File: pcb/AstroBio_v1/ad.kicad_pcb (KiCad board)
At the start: 2 copper layers, 100 x 100 mm, 52 parts, among them J1 POWER 24V, J10 NTC 10k 3950, J12 HEIGHT_SENSOR2, J13 HEIGHT_SENSOR2, J2 Nema17, J3 MS1, J4 MS2, J5 MS2, J6 MS2, J7 FLOW_SENSOR, J8 SERVO, J9 PH_MODUL, U1 ESP32-DevKitC, U2 TBA2-0511, U3 LM3940, U4 LM358

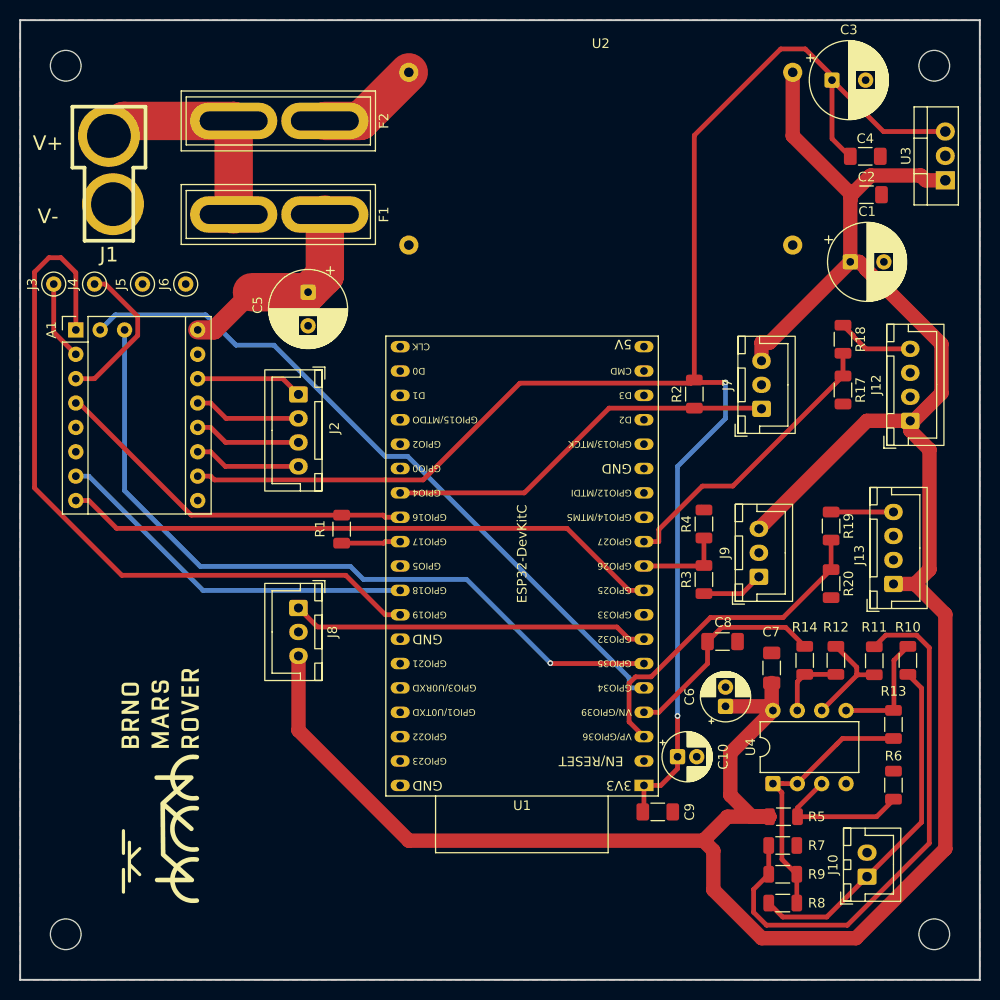
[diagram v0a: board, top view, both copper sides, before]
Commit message: Flip the ESP32 around and generate gerbers
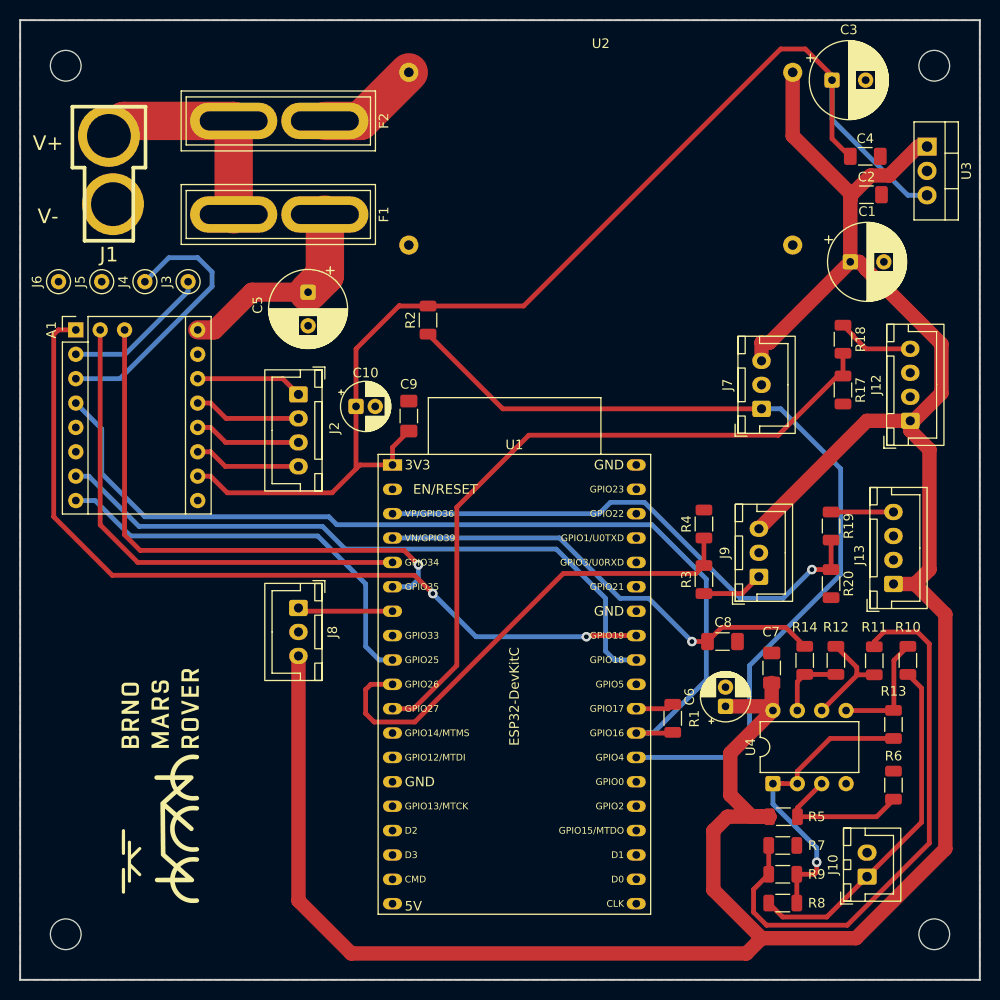
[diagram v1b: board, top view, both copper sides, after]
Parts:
- moved C10 49.5 mm to (76.5, 63.5)
- moved C9 48.7 mm to (82.0, 64.5), turned to 90 degrees
- moved U1 42.4 mm to (80.3, 69.6), turned to 0 degrees
- moved R1 39.7 mm to (109.5, 96.0), turned to -90 degrees
- moved R2 28.8 mm to (84.0, 54.5)
- moved J3 14.0 mm to (59.0, 50.5)
- moved J6 13.3 mm to (45.5, 50.5)
- moved J4 5.26 mm to (54.5, 50.5)
- moved J5 4.26 mm to (50.0, 50.5)
- moved U3 4.00 mm to (136.0, 36.4), turned to -90 degrees
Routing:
- net RX_TMC: track 38.7 -> 100.0 mm
- net SIGNAL_FLOW: track 41.3 -> 93.2 mm
- net +3.3V: track 177.0 -> 129.2 mm, vias 2 -> 0
- net SIGNAL_LEVEL2: track 31.0 -> 73.3 mm
- net SIGNAL_PH: track 9.14 -> 50.8 mm
- net STEP_TMC: track 38.7 -> 69.6 mm
- net SIGNAL_SERVO: track 37.3 -> 9.94 mm
- net SIGNAL_NTC: track 22.6 -> 48.9 mm, vias 0 -> 1
- net DIAG_TMC0: track 74.0 -> 52.4 mm
- net DIAG_TMC1: track 78.3 -> 57.8 mm
- net +5V: track 262.2 -> 282.4 mm
- net SIGNAL_LEVEL1: track 35.5 -> 54.9 mm, vias 0 -> 1
- net DIR_TMC: track 63.1 -> 43.7 mm
- net Net-(A1-MS2): track 16.2 -> 28.3 mm
- net EN_TMC: track 77.6 -> 87.4 mm, vias 0 -> 2
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
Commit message: change the LDO for a smaller one
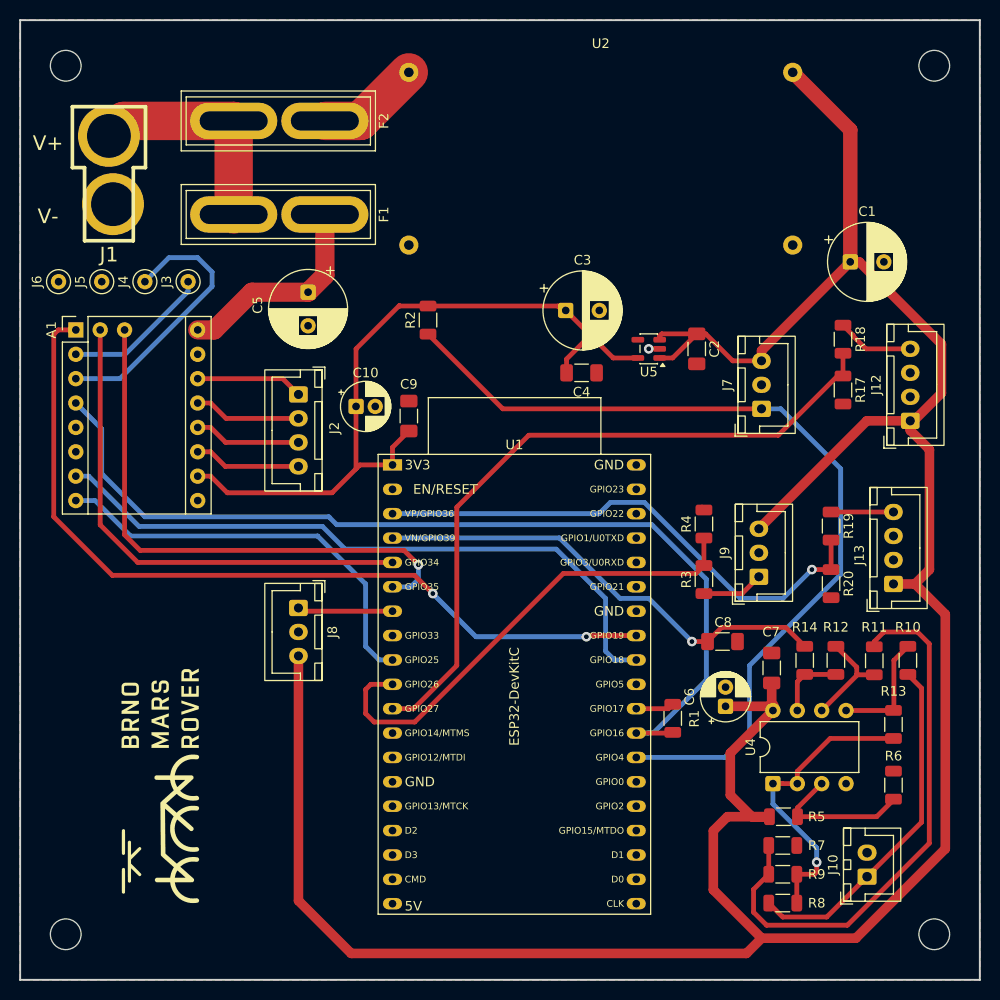
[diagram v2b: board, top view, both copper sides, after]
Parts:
- removed U3: LM3940, Package_TO_SOT_THT:TO-220-3_Vertical
- added U5: TLV75533PDBV, Package_TO_SOT_SMD:SOT-23-5, F.Cu at (107.0, 57.5)
- moved C4 37.2 mm to (100.0, 60.0)
- moved C3 36.7 mm to (98.3, 53.5)
- moved C2 23.9 mm to (112.0, 57.5), turned to -90 degrees
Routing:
- net +3.3V: track 129.2 -> 77.4 mm
- net +5V: track 282.4 -> 289.4 mm
- net GND: track 0.35 -> 1.49 mm, vias 0 -> 1
